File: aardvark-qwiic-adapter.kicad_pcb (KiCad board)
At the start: 2 copper layers, 17.8 x 15.2 mm, 2 parts, among them J1 Conn_02x05_Odd_Even, J2 Conn_01x03

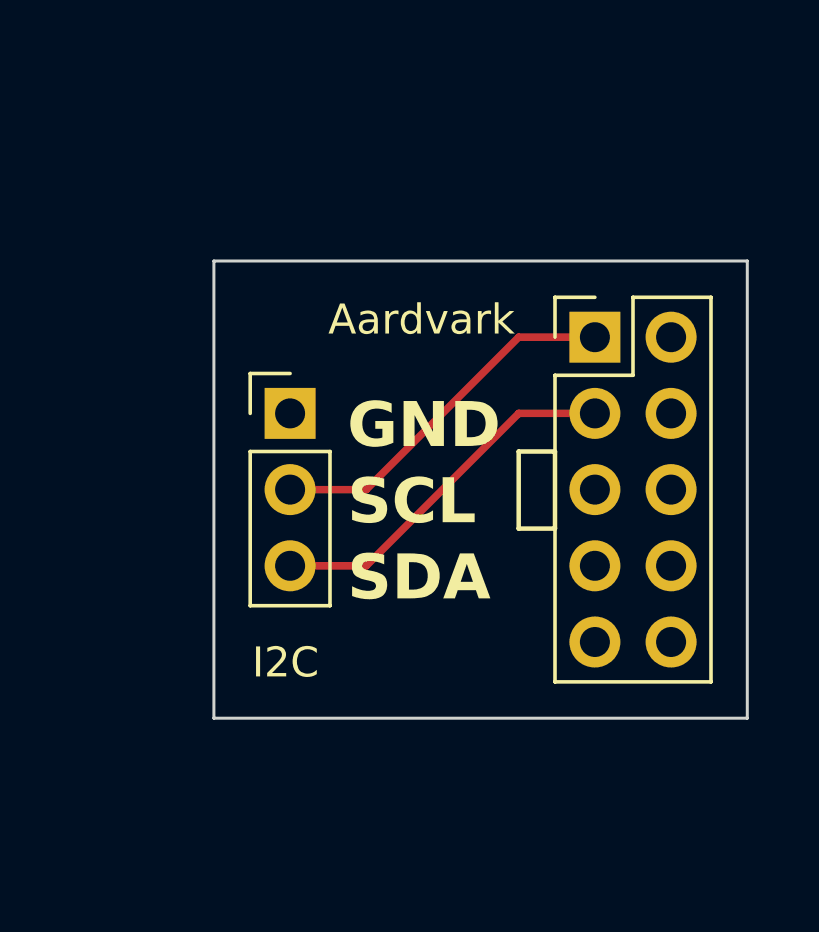
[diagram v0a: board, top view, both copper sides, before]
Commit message: Place components, 3d models
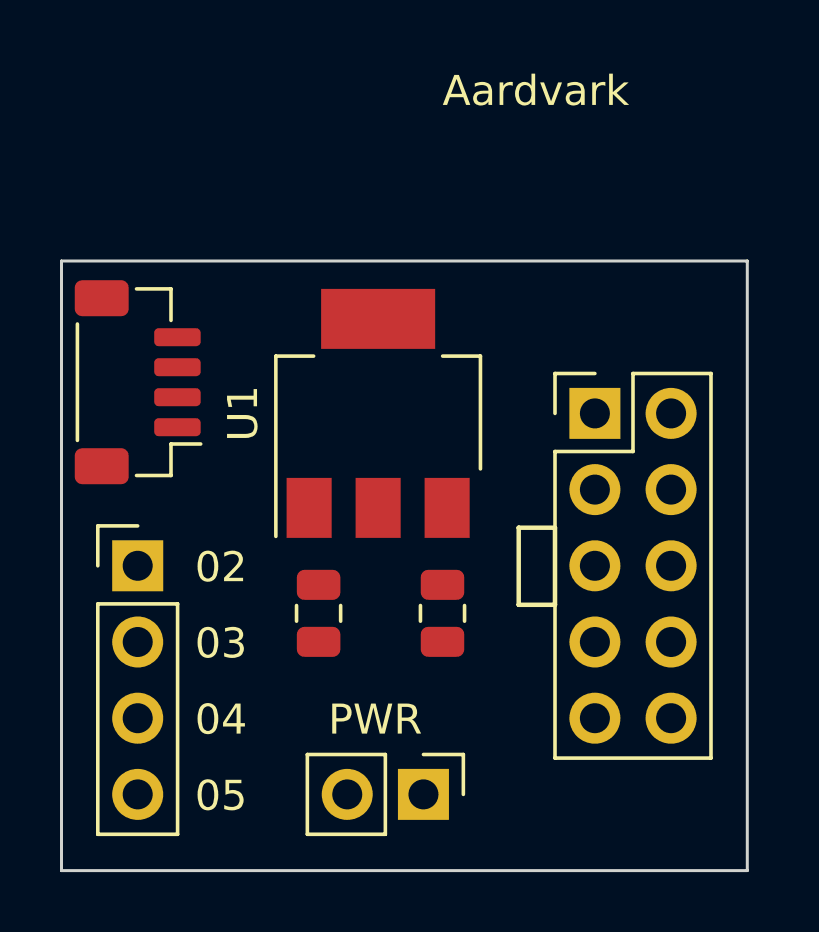
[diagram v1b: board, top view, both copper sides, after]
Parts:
- added C1: 4.7uF, Capacitor_SMD:C_0805_2012Metric, F.Cu at (122.9, 87.9)
- added C2: 4.7uF, Capacitor_SMD:C_0805_2012Metric, F.Cu at (127.0, 87.9)
- added J3: Conn_01x04, Connector_PinHeader_2.54mm:PinHeader_1x04_P2.54mm_Vertical, F.Cu at (116.8, 86.4)
- added J4: Conn_01x02, Connector_PinHeader_2.54mm:PinHeader_1x02_P2.54mm_Vertical, F.Cu at (126.4, 94.0)
- added U1: AP7361C-33E, Package_TO_SOT_SMD:SOT-223-3_TabPin2, F.Cu at (124.9, 81.3)
- J2: value Conn_01x03 -> Conn_01x04; footprint Connector_PinHeader_2.54mm:PinHeader_1x03_P2.54mm_Vertical -> Connector_JST:JST_SH_BM04B-SRSS-TB_1x04-1MP_P1.00mm_Vertical
- moved J2 5.19 mm to (116.8, 80.2), turned to 90 degrees
- moved J1 2.54 mm to (132.1, 81.3)
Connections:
- J1 pad 10: /GND -> GND
- J1 pad 2: /GND -> GND
- J1 pad 4: unconnected-(J1-Pin_4-Pad4) -> +5V
- J1 pad 5: /MISO -> /GPIO02
- J1 pad 6: unconnected-(J1-Pin_6-Pad6) -> +5V
- J1 pad 7: /SCLK -> /GPIO03
- J1 pad 8: /MOSI -> /GPIO04
- J1 pad 9: /SS -> /GPIO05
- J2 pad 1: /GND -> /SCL
- J2 pad 2: /SCL -> /SDA
- J2 pad 3: /SDA -> /PWR
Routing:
- net /SDA: track 12.3 -> 0.00 mm
- net /SCL: track 12.3 -> 0.00 mm
- added copper zone on B.Cu, net GND
- removed copper zone on B.Cu, net /GND
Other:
- board size 17.8 x 15.2 mm -> 22.9 x 20.3 mm
- board text added: "02"
- board text added: "03"
- board text added: "04"
- board text added: "05"
- board text added: "PWR"
- board text removed: "GND"
- board text removed: "I2C"
- board text removed: "SCL"
- board text removed: "SDA"

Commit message: Route
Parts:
- moved J4 1.58 mm to (126.2, 92.4)
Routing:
- net GND: track 0.00 -> 48.3 mm, vias 0 -> 5
- net /GPIO04: track 0.00 -> 30.5 mm
- net /GPIO02: track 0.00 -> 27.2 mm
- net /GPIO03: track 0.00 -> 23.4 mm
- net /SDA: track 0.00 -> 19.7 mm
- net +5V: track 0.00 -> 19.1 mm
- net /GPIO05: track 0.00 -> 17.1 mm
- net /PWR: track 0.00 -> 17.0 mm
- net /SCL: track 0.00 -> 14.1 mm
- net +3.3V: track 0.00 -> 2.63 mm
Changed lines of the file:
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@@
     (property "ki_keywords" "linear regulator ldo fixed positive")
     (attr smd)
-    (fp_text reference "U1" (at 0 -4.5 90) (layer "F.SilkS")
+    (fp_text reference "U1" (at 0 -4.5 90) (layer "F.SilkS") hide
         (effects (font (size 1 1) (thickness 0.15)))
     )
@@
   )
   (footprint "Connector_PinHeader_2.54mm:PinHeader_1x02_P2.54mm_Vertical" (layer "F.Cu")
-    (at 126.365 93.98 -90)
+    (at 126.243 92.4052 -90)
     (descr "Through hole straight pin header, 1x02, 2.54mm pitch, single row")
     (tags "Through hole pin header THT 1x02 2.54mm single row")
@@
     (effects (font (size 1 1) (thickness 0.15)) (justify left bottom))
   )
-  (gr_text "Aardvark" (at 127 71.12) (layer "F.SilkS")
+  (gr_text "Aardvark" (at 129.54 78.8416) (layer "F.SilkS")
     (effects (font (size 1 1) (thickness 0.15)) (justify left bottom))
   )
-  (gr_text "PWR" (at 123.19 92.075) (layer "F.SilkS")
+  (gr_text "PWR" (at 123.4694 95.7072) (layer "F.SilkS")
     (effects (font (size 1 1) (thickness 0.15)) (justify left bottom))
   )
@@
     (effects (font (size 1 1) (thickness 0.15)) (justify left bottom))
   )
+  (segment (start 118.1678 81.7372) (end 118.165 81.74) (width 0.25) (layer "F.Cu") (net 1))
+  (segment (start 124.968 81.28) (end 124.5108 81.7372) (width 0.25) (layer "F.Cu") (net 1))
+  (segment (start 124.5108 81.7372) (end 118.1678 81.7372) (width 0.25) (layer "F.Cu") (net 1))
+  (segment (start 132.08 81.28) (end 124.968 81.28) (width 0.25) (layer "F.Cu") (net 1))
+  (segment (start 132.08 83.82) (end 133.445 82.455) (width 0.25) (layer "F.Cu") (net 2))
+  (segment (start 133.445 80.295) (end 133.2362 80.0862) (width 0.25) (layer "F.Cu") (net 2))
+  (segment (start 133.2362 80.0862) (end 119.5578 80.0862) (width 0.25) (layer "F.Cu") (net 2))
+  (segment (start 118.904 80.74) (end 118.165 80.74) (width 0.25) (layer "F.Cu") (net 2))
+  (segment (start 133.445 82.455) (end 133.445 80.295) (width 0.25) (layer "F.Cu") (net 2))
+  (segment (start 119.5578 80.0862) (end 118.904 80.74) (width 0.25) (layer "F.Cu") (net 2))
+  (segment (start 118.165 78.74) (end 119.761 78.74) (width 0.25) (layer "F.Cu") (net 3))
+  (segment (start 122.87 88.895) (end 122.87 90.1294) (width 0.25) (layer "F.Cu") (net 3))
+  (segment (start 122.87 90.1294) (end 122.8852 90.1446) (width 0.25) (layer "F.Cu") (net 3))
+  (segment (start 124.855 78.13) (end 127.61 78.13) (width 0.25) (layer "F.Cu") (net 3))
+  (segment (start 127.61 78.13) (end 127.635 78.105) (width 0.25) (layer "F.Cu") (net 3))
+  (segment (start 124.855 86.1428) (end 124.841 86.1568) (width 0.25) (layer "F.Cu") (net 3))
+  (segment (start 124.855 84.43) (end 124.855 86.1428) (width 0.25) (layer "F.Cu") (net 3))
+  (segment (start 127 88.895) (end 127 90.0938) (width 0.25) (layer "F.Cu") (net 3))
+  (via (at 127.635 78.105) (size 0.8) (drill 0.4) (layers "F.Cu" "B.Cu") (net 3))
+  (via (at 122.8852 90.1446) (size 0.8) (drill 0.4) (layers "F.Cu" "B.Cu") (net 3))
+  (via (at 127 90.0938) (size 0.8) (drill 0.4) (layers "F.Cu" "B.Cu") (net 3))
+  (via (at 119.761 78.74) (size 0.8) (drill 0.4) (layers "F.Cu" "B.Cu") (net 3))
+  (via (at 124.841 86.1568) (size 0.8) (drill 0.4) (layers "F.Cu" "B.Cu") (net 3))
+  (segment (start 122.8852 90.1446) (end 124.841 88.1888) (width 0.25) (layer "B.Cu") (net 3))
+  (segment (start 134.62 78.105) (end 134.62 81.28) (width 0.25) (layer "B.Cu") (net 3))
+  (segment (start 133.445 82.455) (end 134.62 81.28) (width 0.25) (layer "B.Cu") (net 3))
+  (segment (start 124.841 88.1888) (end 124.841 86.1568) (width 0.25) (layer "B.Cu") (net 3))
+  (segment (start 127 78.74) (end 127.635 78.105) (width 0.25) (layer "B.Cu") (net 3))
+  (segment (start 124.841 87.9348) (end 124.841 86.1568) (width 0.25) (layer "B.Cu") (net 3))
+  (segment (start 124.841 86.1568) (end 128.081499 86.1568) (width 0.25) (layer "B.Cu") (net 3))
+  (segment (start 119.761 78.74) (end 127 78.74) (width 0.25) (layer "B.Cu") (net 3))
+  (segment (start 128.081499 86.1568) (end 131.783299 82.455) (width 0.25) (layer "B.Cu") (net 3))
+  (segment (start 127.635 78.105) (end 134.62 78.105) (width 0.25) (layer "B.Cu") (net 3))
+  (segment (start 127 90.0938) (end 124.841 87.9348) (width 0.25) (layer "B.Cu") (net 3))
+  (segment (start 131.783299 82.455) (end 133.445 82.455) (width 0.25) (layer "B.Cu") (net 3))
+  (segment (start 127.155 86.84) (end 127 86.995) (width 0.25) (layer "F.Cu") (net 4))
+  (segment (start 127.155 84.43) (end 127.155 86.84) (width 0.25) (layer "F.Cu") (net 4))
+  (segment (start 121.0564 91.8718) (end 121.0564 87.2998) (width 0.25) (layer "F.Cu") (net 5))
+  (segment (start 120.1166 86.36) (end 116.84 86.36) (width 0.25) (layer "F.Cu") (net 5))
+  (segment (start 129.4892 86.36) (end 128.8542 86.995) (width 0.25) (layer "F.Cu") (net 5))
+  (segment (start 123.052 93.8674) (end 121.0564 91.8718) (width 0.25) (layer "F.Cu") (net 5))
+  (segment (start 127.1308 93.8674) (end 123.052 93.8674) (width 0.25) (layer "F.Cu") (net 5))
+  (segment (start 128.8542 86.995) (end 128.8542 92.144) (width 0.25) (layer "F.Cu") (net 5))
+  (segment (start 121.0564 87.2998) (end 120.1166 86.36) (width 0.25) (layer "F.Cu") (net 5))
+  (segment (start 128.8542 92.144) (end 127.1308 93.8674) (width 0.25) (layer "F.Cu") (net 5))
+  (segment (start 132.08 86.36) (end 129.4892 86.36) (width 0.25) (layer "F.Cu") (net 5))
+  (segment (start 120.3452 92.4306) (end 120.3452 89.281) (width 0.25) (layer "F.Cu") (net 6))
+  (segment (start 130.0734 92.075) (end 127.831 94.3174) (width 0.25) (layer "F.Cu") (net 6))
+  (segment (start 127.831 94.3174) (end 122.232 94.3174) (width 0.25) (layer "F.Cu") (net 6))
+  (segment (start 132.08 88.9) (end 132.0292 88.9508) (width 0.25) (layer "F.Cu") (net 6))
+  (segment (start 132.0292 88.9508) (end 130.0734 88.9508) (width 0.25) (layer "F.Cu") (net 6))
+  (segment (start 130.0734 88.9508) (end 130.0734 92.075) (width 0.25) (layer "F.Cu") (net 6))
+  (segment (start 122.232 94.3174) (end 120.3452 92.4306) (width 0.25) (layer "F.Cu") (net 6))
+  (segment (start 119.9642 88.9) (end 116.84 88.9) (width 0.25) (layer "F.Cu") (net 6))
+  (segment (start 120.3452 89.281) (end 119.9642 88.9) (width 0.25) (layer "F.Cu") (net 6))
+  (segment (start 136.0424 92.4052) (end 132.8674 95.5802) (width 0.25) (layer "F.Cu") (net 7))
+  (segment (start 134.62 88.9) (end 136.0424 90.3224) (width 0.25) (layer "F.Cu") (net 7))
+  (segment (start 116.1014 95.5802) (end 115.2144 94.6932) (width 0.25) (layer "F.Cu") (net 7))
+  (segment (start 136.0424 90.3224) (end 136.0424 92.4052) (width 0.25) (layer "F.Cu") (net 7))
+  (segment (start 115.2144 94.6932) (end 115.2144 93.0656) (width 0.25) (layer "F.Cu") (net 7))
+  (segment (start 132.8674 95.5802) (end 116.1014 95.5802) (width 0.25) (layer "F.Cu") (net 7))
+  (segment (start 115.2144 93.0656) (end 116.84 91.44) (width 0.25) (layer "F.Cu") (net 7))
+  (segment (start 132.08 91.44) (end 128.524 94.996) (width 0.25) (layer "F.Cu") (net 8))
+  (segment (start 128.524 94.996) (end 117.856 94.996) (width 0.25) (layer "F.Cu") (net 8))
+  (segment (start 117.856 94.996) (end 116.84 93.98) (width 0.25) (layer "F.Cu") (net 8))
+  (segment (start 121.82 90.5222) (end 123.703 92.4052) (width 0.25) (layer "F.Cu") (net 9))
+  (segment (start 116.5352 81.8388) (end 121.82 87.1236) (width 0.25) (layer "F.Cu") (net 9))
+  (segment (start 117.0338 79.74) (end 116.5352 80.2386) (width 0.25) (layer "F.Cu") (net 9))
+  (segment (start 118.165 79.74) (end 117.0338 79.74) (width 0.25) (layer "F.Cu") (net 9))
+  (segment (start 116.5352 80.2386) (end 116.5352 81.8388) (width 0.25) (layer "F.Cu") (net 9))
+  (segment (start 121.82 87.1236) (end 121.82 90.5222) (width 0.25) (layer "F.Cu") (net 9))
+  (segment (start 123.2408 82.8802) (end 122.555 83.566) (width 0.25) (layer "F.Cu") (net 10))
+  (segment (start 134.62 83.82) (end 133.445 84.995) (width 0.25) (layer "F.Cu") (net 10))
+  (segment (start 133.445 85.185) (end 133.445 84.995) (width 0.25) (layer "F.Cu") (net 10))
+  (segment (start 134.62 86.36) (end 133.445 85.185) (width 0.25) (layer "F.Cu") (net 10))
+  (segment (start 133.445 84.995) (end 130.12 84.995) (width 0.25) (layer "F.Cu") (net 10))
+  (segment (start 128.0052 82.8802) (end 123.2408 82.8802) (width 0.25) (layer "F.Cu") (net 10))
+  (segment (start 122.555 83.566) (end 122.555 84.43) (width 0.25) (layer "F.Cu") (net 10))
+  (segment (start 130.12 84.995) (end 128.0052 82.8802) (width 0.25) (layer "F.Cu") (net 10))
+  (segment (start 122.555 86.68) (end 122.87 86.995) (width 0.25) (layer "F.Cu") (net 10))
+  (segment (start 122.555 84.43) (end 122.555 86.68) (width 0.25) (layer "F.Cu") (net 10))
   (zone (net 3) (net_name "GND") (layer "B.Cu") (hatch edge 0.5)
     (connect_pads (clearance 0.5))
